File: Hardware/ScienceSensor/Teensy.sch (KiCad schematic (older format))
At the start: 1 part

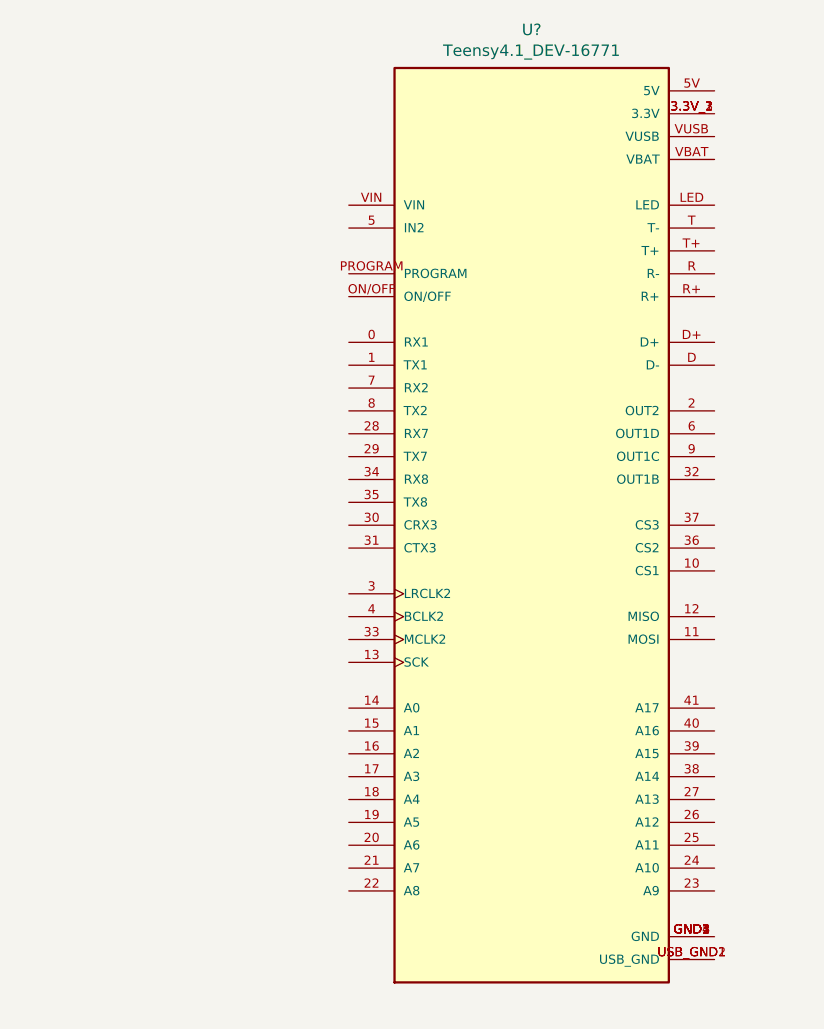
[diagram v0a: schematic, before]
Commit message: Teensy wiring
some labels added for teensy
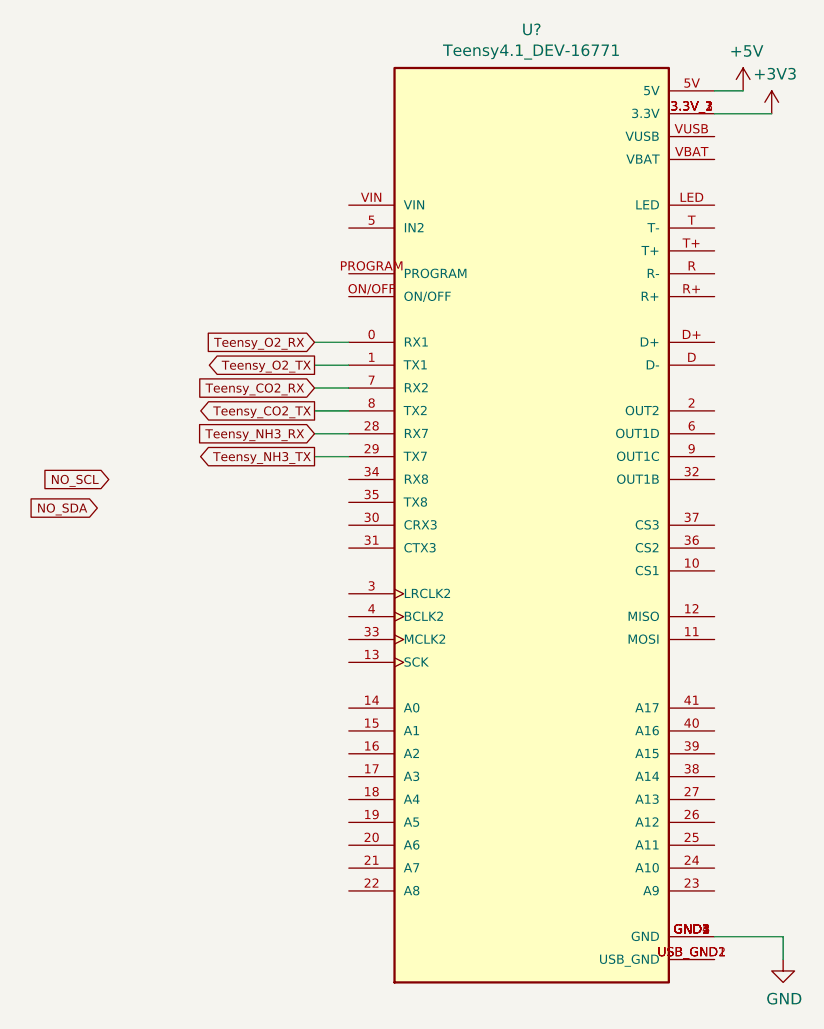
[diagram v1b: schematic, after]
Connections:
- net Teensy_O2_RX: now reaches U?.0 (RX1)
- net Teensy_O2_TX: now reaches U?.1 (TX1)
- net Teensy_NH3_RX: now reaches U?.28 (RX7)
- net Teensy_NH3_TX: now reaches U?.29 (TX7)
- net +3V3: now reaches U?.3.3V_1 (3.3V), U?.3.3V_2 (3.3V), U?.3.3V_3 (3.3V)
- net +5V: now reaches U?.5V
- net Teensy_CO2_RX: now reaches U?.7 (RX2)
- net Teensy_CO2_TX: now reaches U?.8 (TX2)
- net GND: now reaches U?.GND1 (GND), U?.GND2 (GND), U?.GND3 (GND), U?.GND4 (GND), U?.GND5 (GND)
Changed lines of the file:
@@
 	1    0    0    -1
 $EndComp
+Text GLabel 2625 2700 0    39   Input ~ 0
+Teensy_O2_RX
+Text GLabel 2625 2900 0    39   Input ~ 0
+Teensy_CO2_RX
+Text GLabel 2625 3100 0    39   Input ~ 0
+Teensy_NH3_RX
+Text GLabel 1725 3300 0    39   Input ~ 0
+NO_SCL
+Text GLabel 1675 3425 0    39   Input ~ 0
+NO_SDA
+Text GLabel 2625 3000 0    39   Output ~ 0
+Teensy_CO2_TX
+Text GLabel 2625 2800 0    39   Output ~ 0
+Teensy_O2_TX
+Text GLabel 2625 3200 0    39   Output ~ 0
+Teensy_NH3_TX
+Wire Wire Line
+	2775 2700 2625 2700
+Wire Wire Line
+	2625 2800 2775 2800
+Wire Wire Line
+	2625 2900 2775 2900
+Wire Wire Line
+	2625 3000 2775 3000
+Wire Wire Line
+	2625 3100 2775 3100
+Wire Wire Line
+	2625 3200 2775 3200
+$Comp
+L power:+5V #PWR?
+U 1 1 6323FF98
+P 4500 1600
+F 0 "#PWR?" H 4500 1450 50  0001 C CNN
+F 1 "+5V" H 4515 1773 50  0000 C CNN
+F 2 "" H 4500 1600 50  0001 C CNN
+F 3 "" H 4500 1600 50  0001 C CNN
+	1    4500 1600
+	1    0    0    -1
+$EndComp
+$Comp
+L power:+3V3 #PWR?
+U 1 1 632404BA
+P 4625 1700
+F 0 "#PWR?" H 4625 1550 50  0001 C CNN
+F 1 "+3V3" H 4640 1873 50  0000 C CNN
+F 2 "" H 4625 1700 50  0001 C CNN
+F 3 "" H 4625 1700 50  0001 C CNN
+	1    4625 1700
+	1    0    0    -1
+$EndComp
+$Comp
+L power:GND #PWR?
+U 1 1 63241160
+P 4675 5400
+F 0 "#PWR?" H 4675 5150 50  0001 C CNN
+F 1 "GND" H 4680 5227 50  0000 C CNN
+F 2 "" H 4675 5400 50  0001 C CNN
+F 3 "" H 4675 5400 50  0001 C CNN
+	1    4675 5400
+	1    0    0    -1
+$EndComp
+Wire Wire Line
+	4375 5300 4675 5300
+Wire Wire Line
+	4675 5300 4675 5400
+Wire Wire Line
+	4375 1600 4500 1600
+Wire Wire Line
+	4625 1700 4375 1700
 $EndSCHEMATC

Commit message: Teensy Connections
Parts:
- added C?: 0.1uF, symbol Device:C
- added D? (x3): Blue, symbol Device:LED
- added J?: RJ45_LED_Shielded, symbol Connector:RJ45_LED_Shielded
- added J?: 6P6C, symbol Connector:6P6C
- added R? (x3): 130, symbol Device:R
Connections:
- net GND: now also D?.1 (K), D?.1 (K), D?.1 (K), J?.SH
- net Teensy_NO2_CS: now reaches U?.10 (CS1)
- net Teensy_NO2_MISO: now reaches U?.12 (MISO)
- net Teensy_NO2_SCK: now reaches U?.13 (SCK)
- net Laser_1: now reaches U?.14 (A0)
- net Laser_2: now reaches U?.15 (A1)
- net Laser_3: now reaches U?.16 (A2)
- net UV_Lights: now reaches U?.18 (A4)
- net Lights: now reaches U?.19 (A5)
- net at U?.20 (A6): now also R?.1
- net at U?.21 (A7): now also R?.1
- net at U?.22 (A8): now also R?.1
- net Photodiode_3: now reaches U?.23 (A9)
- net Photodiode_2: now reaches U?.24 (A10)
- net Photodiode_1: now reaches U?.25 (A11)
- net NO_Ref: now reaches U?.40 (A16)
- net NO_Gas: now reaches U?.41 (A17)
- net Teensy_NH3_RX: no longer names the net of U?.28 (RX7)
- net Teensy_NH3_TX: no longer names the net of U?.29 (TX7)
- new net: D?.2 (A), R?.2 (x3)
- new net: J?.1, J?.1
- new net: J?.10, J?.4
- new net: C?.1, J?.2, J?.5
- new net: J?.2, J?.3
- new net: J?.4, J?.6
- new net: J?.5, J?.6
- new net: C?.2, J?.3, J?.8, J?.9
- no-connect marks 0 -> 38
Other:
- note added: "Software Signals"
